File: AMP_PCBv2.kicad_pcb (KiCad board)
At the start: 2 copper layers, 2 parts, among them U1 Teensy4.0, U2 Logo

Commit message: Route PCB
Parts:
- added C1: 47pF, Capacitor_SMD:C_0805_2012Metric_Pad1.18x1.45mm_HandSolder, F.Cu at (145.3, 134.6)
- added C10: 0.1uF, Capacitor_SMD:C_0805_2012Metric_Pad1.18x1.45mm_HandSolder, F.Cu at (177.5, 136.8)
- added C11: 0.1uF, Capacitor_SMD:C_0805_2012Metric_Pad1.18x1.45mm_HandSolder, F.Cu at (178.5, 108.6)
- added C12: 0.1uF, Capacitor_SMD:C_0805_2012Metric_Pad1.18x1.45mm_HandSolder, F.Cu at (181.1, 103.7)
- added C13: 0.1uF, Capacitor_SMD:C_0805_2012Metric_Pad1.18x1.45mm_HandSolder, F.Cu at (109.5, 135.6)
- added C14: 0.1uF, Capacitor_SMD:C_0805_2012Metric_Pad1.18x1.45mm_HandSolder, F.Cu at (138.5, 110.9)
- added C15: 0.1uF, Capacitor_SMD:C_0805_2012Metric_Pad1.18x1.45mm_HandSolder, F.Cu at (138.5, 96.7)
- added C16: 0.1uF, Capacitor_SMD:C_0805_2012Metric_Pad1.18x1.45mm_HandSolder, F.Cu at (164.6, 83.8)
- added C17: 0.1uF, Capacitor_SMD:C_0805_2012Metric_Pad1.18x1.45mm_HandSolder, F.Cu at (156.7, 62.5)
- added C18: 0.1uF, Capacitor_SMD:C_0805_2012Metric_Pad1.18x1.45mm_HandSolder, F.Cu at (176.8, 63.2)
- added C2: 47pF, Capacitor_SMD:C_0805_2012Metric_Pad1.18x1.45mm_HandSolder, F.Cu at (145.3, 136.9)
- added C3: 4.7uF, Capacitor_SMD:C_0805_2012Metric_Pad1.18x1.45mm_HandSolder, F.Cu at (144.9, 131.3)
- added C4: 100nF, Capacitor_SMD:C_0805_2012Metric_Pad1.18x1.45mm_HandSolder, F.Cu at (142.7, 131.3)
- added C5: 100nF, Capacitor_SMD:C_0805_2012Metric_Pad1.18x1.45mm_HandSolder, F.Cu at (140.5, 131.3)
- added C6: 10uF, Capacitor_SMD:C_0805_2012Metric_Pad1.18x1.45mm_HandSolder, F.Cu at (154.7, 94.7)
- added C7: 10uF, Capacitor_SMD:C_0805_2012Metric_Pad1.18x1.45mm_HandSolder, F.Cu at (168.9, 94.7)
- added C8: 10nF, Capacitor_SMD:C_0805_2012Metric_Pad1.18x1.45mm_HandSolder, F.Cu at (156.7, 81.3)
- added C9: 0.1uF, Capacitor_SMD:C_0805_2012Metric_Pad1.18x1.45mm_HandSolder, F.Cu at (180.3, 132.0)
- added D1: GN, LED_THT:LED_D5.0mm, F.Cu at (172.7, 120.1)
- added D10: YL, LED_THT:LED_D5.0mm, F.Cu at (134.6, 88.9)
- added D11: RD, LED_THT:LED_D5.0mm, F.Cu at (134.6, 80.3)
- added D12: RD, LED_THT:LED_D5.0mm, F.Cu at (134.6, 71.6)
- added D13: RD, LED_THT:LED_D5.0mm, F.Cu at (161.0, 68.6)
- added D2: GN, LED_THT:LED_D5.0mm, F.Cu at (179.3, 120.1)
- added D3: GN, LED_THT:LED_D5.0mm, F.Cu at (185.9, 122.6)
- added D4: YL, LED_THT:LED_D5.0mm, F.Cu at (187.7, 94.2)
- added D5: YL, LED_THT:LED_D5.0mm, F.Cu at (187.7, 83.8)
- added D6: YL, LED_THT:LED_D5.0mm, F.Cu at (187.7, 73.4)
- added D7: YL, LED_THT:LED_D5.0mm, F.Cu at (187.7, 63.0)
- added D8: YL, LED_THT:LED_D5.0mm, F.Cu at (148.1, 92.5)
- added D9: YL, LED_THT:LED_D5.0mm, F.Cu at (175.5, 92.5)
- added J1: POWER, Connector_Molex:Molex_Mini-Fit_Jr_5566-02A_2x01_P4.20mm_Vertical, F.Cu at (106.7, 45.7)
- added J2: EBRAKE, Connector_Molex:Molex_Mini-Fit_Jr_5566-02A_2x01_P4.20mm_Vertical, F.Cu at (116.8, 45.7)
- added J3: MC, Connector_Molex:Molex_Mini-Fit_Jr_5566-08A_2x04_P4.20mm_Vertical, F.Cu at (139.6, 51.2)
- added J4: STEERING, Connector_Molex:Molex_Mini-Fit_Jr_5566-08A_2x04_P4.20mm_Vertical, F.Cu at (177.8, 51.2)
- added J5: OLED Breakout, Connector_PinSocket_2.54mm:PinSocket_1x04_P2.54mm_Vertical, F.Cu at (102.4, 124.5)
- added J6: EBRAKE_BREAKOUT, AMP:AMP_Brake_Controller_Breakout, F.Cu at (130.0, 96.2)
- added JP1: 5VOB, Jumper:SolderJumper-2_P1.3mm_Open_TrianglePad1.0x1.5mm, F.Cu at (177.5, 131.7)
- added JP10: Jumper_EBRAKE2, Connector_PinHeader_2.54mm:PinHeader_1x03_P2.54mm_Vertical, F.Cu at (161.6, 101.0)
- added JP11: 0.25s, Jumper:SolderJumper-2_P1.3mm_Open_TrianglePad1.0x1.5mm, F.Cu at (156.5, 65.5)
- added JP12: 1s, Jumper:SolderJumper-2_P1.3mm_Open_TrianglePad1.0x1.5mm, F.Cu at (156.5, 68.3)
- added JP13: 2s, Jumper:SolderJumper-2_P1.3mm_Open_TrianglePad1.0x1.5mm, F.Cu at (156.5, 71.1)
- added JP14: 4s, Jumper:SolderJumper-2_P1.3mm_Open_TrianglePad1.0x1.5mm, F.Cu at (156.5, 73.9)
- added JP2: 3V3OB, Jumper:SolderJumper-2_P1.3mm_Open_TrianglePad1.0x1.5mm, F.Cu at (181.1, 108.8)
- added JP3: Jumper_FS1, Connector_PinHeader_2.54mm:PinHeader_1x03_P2.54mm_Vertical, F.Cu at (161.6, 118.8)
- added JP4: Jumper_FWD, Connector_PinHeader_2.54mm:PinHeader_1x03_P2.54mm_Vertical, F.Cu at (161.6, 116.2)
- added JP5: Jumper_REV, Connector_PinHeader_2.54mm:PinHeader_1x03_P2.54mm_Vertical, F.Cu at (161.6, 113.7)
- added JP6: Jumper_THROTTLE, Connector_PinHeader_2.54mm:PinHeader_1x03_P2.54mm_Vertical, F.Cu at (161.6, 111.2)
- added JP7: Jumper_RB, Connector_PinHeader_2.54mm:PinHeader_1x03_P2.54mm_Vertical, F.Cu at (161.6, 108.6)
- added JP8: Jumper_STEERING, Connector_PinHeader_2.54mm:PinHeader_1x03_P2.54mm_Vertical, F.Cu at (161.6, 106.1)
- added JP9: Jumper_EBRAKE1, Connector_PinHeader_2.54mm:PinHeader_1x03_P2.54mm_Vertical, F.Cu at (161.6, 103.5)
- added JT1: Conn_01x14_Male, Connector_PinHeader_2.54mm:PinHeader_1x14_P2.54mm_Vertical, F.Cu at (132.1, 137.2)
- added JT2: Conn_01x05_Male, Connector_PinHeader_2.54mm:PinHeader_1x05_P2.54mm_Vertical, F.Cu at (124.5, 99.1)
- added JT3: Conn_01x14_Male, Connector_PinHeader_2.54mm:PinHeader_1x14_P2.54mm_Vertical, F.Cu at (106.7, 104.1)
- added JT4: Conn_01x01_Male, Connector_PinHeader_2.54mm:PinHeader_1x01_P2.54mm_Vertical, F.Cu at (104.1, 134.6)
- added JX1: MC_OLD, Connector_Molex:Molex_KK-254_AE-6410-04A_1x04_P2.54mm_Vertical, F.Cu at (147.3, 44.5)
- added Q1: Q_NMOS_GDS, Package_TO_SOT_THT:TO-251-3_Vertical, F.Cu at (181.5, 98.5)
- added Q2: Q_NMOS_GDS, Package_TO_SOT_THT:TO-251-3_Vertical, F.Cu at (181.5, 88.1)
- added Q3: Q_NMOS_GDS, Package_TO_SOT_THT:TO-251-3_Vertical, F.Cu at (181.5, 77.7)
- added Q4: Q_NMOS_GDS, Package_TO_SOT_THT:TO-251-3_Vertical, F.Cu at (181.5, 67.3)
- added R1: 560, Resistor_SMD:R_0805_2012Metric_Pad1.20x1.40mm_HandSolder, F.Cu at (171.4, 117.0)
- added R10: 130, Resistor_SMD:R_0805_2012Metric_Pad1.20x1.40mm_HandSolder, F.Cu at (178.0, 117.0)
- added R11: 56, Resistor_SMD:R_0805_2012Metric_Pad1.20x1.40mm_HandSolder, F.Cu at (184.6, 117.0)
- added R12: 56, Resistor_SMD:R_0805_2012Metric_Pad1.20x1.40mm_HandSolder, F.Cu at (188.7, 98.8)
- added R13: 1K, Resistor_SMD:R_0805_2012Metric_Pad1.20x1.40mm_HandSolder, F.Cu at (184.9, 98.8)
- added R14: 56, Resistor_SMD:R_0805_2012Metric_Pad1.20x1.40mm_HandSolder, F.Cu at (151.6, 87.1)
- added R15: 1K, Resistor_SMD:R_0805_2012Metric_Pad1.20x1.40mm_HandSolder, F.Cu at (154.7, 92.7)
- added R16: 1K, Resistor_SMD:R_0805_2012Metric_Pad1.20x1.40mm_HandSolder, F.Cu at (154.7, 88.1)
- added R17: 56, Resistor_SMD:R_0805_2012Metric_Pad1.20x1.40mm_HandSolder, F.Cu at (188.7, 88.4)
- added R18: 1K, Resistor_SMD:R_0805_2012Metric_Pad1.20x1.40mm_HandSolder, F.Cu at (184.9, 88.4)
- added R19: 1.8K, Resistor_SMD:R_0805_2012Metric_Pad1.20x1.40mm_HandSolder, F.Cu at (154.7, 86.1)
- added R2: 27, Resistor_SMD:R_0805_2012Metric_Pad1.20x1.40mm_HandSolder, F.Cu at (141.2, 134.6)
- added R20: 10K, Resistor_SMD:R_0805_2012Metric_Pad1.20x1.40mm_HandSolder, F.Cu at (138.5, 123.1)
- added R21: 10K, Resistor_SMD:R_0805_2012Metric_Pad1.20x1.40mm_HandSolder, F.Cu at (138.5, 108.9)
- added R22: 56, Resistor_SMD:R_0805_2012Metric_Pad1.20x1.40mm_HandSolder, F.Cu at (188.7, 78.0)
- added R23: 1K, Resistor_SMD:R_0805_2012Metric_Pad1.20x1.40mm_HandSolder, F.Cu at (184.9, 78.0)
- added R24: 56, Resistor_SMD:R_0805_2012Metric_Pad1.20x1.40mm_HandSolder, F.Cu at (172.0, 87.1)
- added R25: 1K, Resistor_SMD:R_0805_2012Metric_Pad1.20x1.40mm_HandSolder, F.Cu at (168.9, 92.7)
- added R26: 1K, Resistor_SMD:R_0805_2012Metric_Pad1.20x1.40mm_HandSolder, F.Cu at (168.9, 88.1)
- added R27: 1.8K, Resistor_SMD:R_0805_2012Metric_Pad1.20x1.40mm_HandSolder, F.Cu at (168.9, 86.1)
- added R28: 56, Resistor_SMD:R_0805_2012Metric_Pad1.20x1.40mm_HandSolder, F.Cu at (188.7, 67.5)
- added R29: 1K, Resistor_SMD:R_0805_2012Metric_Pad1.20x1.40mm_HandSolder, F.Cu at (184.9, 67.5)
- added R3: 10K, Resistor_SMD:R_0805_2012Metric_Pad1.20x1.40mm_HandSolder, F.Cu at (171.4, 131.0)
- added R30: 1K, Resistor_SMD:R_0805_2012Metric_Pad1.20x1.40mm_HandSolder, F.Cu at (181.1, 60.2)
- added R31: 15K, Resistor_SMD:R_0805_2012Metric_Pad1.20x1.40mm_HandSolder, F.Cu at (156.7, 79.2)
- added R32: 6.2K, Resistor_SMD:R_0805_2012Metric_Pad1.20x1.40mm_HandSolder, F.Cu at (156.7, 77.2)
- added R33: 10K, Resistor_SMD:R_0805_2012Metric_Pad1.20x1.40mm_HandSolder, F.Cu at (164.6, 63.2)
- added R34: 10K, Resistor_SMD:R_0805_2012Metric_Pad1.20x1.40mm_HandSolder, F.Cu at (164.6, 73.9)
- added R35: 33, Resistor_SMD:R_0805_2012Metric_Pad1.20x1.40mm_HandSolder, F.Cu at (162.6, 73.9)
- added R36: 33, Resistor_SMD:R_0805_2012Metric_Pad1.20x1.40mm_HandSolder, F.Cu at (134.4, 67.3)
- added R37: 33, Resistor_SMD:R_0805_2012Metric_Pad1.20x1.40mm_HandSolder, F.Cu at (134.4, 75.9)
- added R38: 56, Resistor_SMD:R_0805_2012Metric_Pad1.20x1.40mm_HandSolder, F.Cu at (134.3, 84.6)
- added R4: 10K, Resistor_SMD:R_0805_2012Metric_Pad1.20x1.40mm_HandSolder, F.Cu at (187.2, 109.6)
- added R5: 3.3K, Resistor_SMD:R_0805_2012Metric_Pad1.20x1.40mm_HandSolder, F.Cu at (174.7, 132.0)
- added R6: 6.2K, Resistor_SMD:R_0805_2012Metric_Pad1.20x1.40mm_HandSolder, F.Cu at (183.9, 108.6)
- added R7: 27, Resistor_SMD:R_0805_2012Metric_Pad1.20x1.40mm_HandSolder, F.Cu at (141.2, 136.9)
- added R8: 4.7K, Resistor_SMD:R_0805_2012Metric_Pad1.20x1.40mm_HandSolder, F.Cu at (142.7, 127.0)
- added R9: 10K, Resistor_SMD:R_0805_2012Metric_Pad1.20x1.40mm_HandSolder, F.Cu at (138.7, 127.0)
- added REF**: MountingHole_3.2mm_M3, MountingHole:MountingHole_3.2mm_M3, F.Cu at (96.5, 45.7)
- added REF**: MountingHole_3.2mm_M3, MountingHole:MountingHole_3.2mm_M3, F.Cu at (96.5, 134.6)
- added REF**: MountingHole_3.2mm_M3, MountingHole:MountingHole_3.2mm_M3, F.Cu at (185.4, 45.7)
- added REF**: MountingHole_3.2mm_M3, MountingHole:MountingHole_3.2mm_M3, F.Cu at (185.4, 134.6)
- added U3: LM1117-ADJ, Package_TO_SOT_THT:TO-220-3_Vertical, F.Cu at (172.2, 128.2)
- added U4: LM1117-ADJ, Package_TO_SOT_THT:TO-220-3_Vertical, F.Cu at (186.4, 112.4)
- added U5: 74HC157, Package_DIP:DIP-16_W7.62mm, F.Cu at (138.0, 120.8)
- added U6: 74HC157, Package_DIP:DIP-16_W7.62mm, F.Cu at (138.0, 106.6)
- added U7: 74HC4060, Package_DIP:DIP-16_W7.62mm, F.Cu at (145.8, 63.0)
- added U8: 74HC00, Package_DIP:DIP-14_W7.62mm, F.Cu at (166.9, 63.0)
- added U9: TLV272, Package_DIP:DIP-8_W7.62mm, F.Cu at (158.0, 86.6)
- added USB1: USB_B, Connector_USB:USB_B_TE_5787834_Vertical, F.Cu at (157.0, 128.8)
- U2: value Logo -> FT234XD; footprint AMP:Logo -> Package_DFN_QFN:DFN-12-1EP_3x3mm_P0.5mm_EP1.6x2.5mm
- moved U2 47.2 mm to (136.9, 133.1), turned to 180 degrees
- moved U1 35.9 mm to (119.4, 120.7), turned to 90 degrees
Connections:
- U1 pad 1: unconnected-(U1-Pad1) -> GND
- U1 pad 10: unconnected-(U1-Pad10) -> /MCU_EBRAKE1
- U1 pad 11: unconnected-(U1-Pad11) -> /MCU_EBRAKE2
- U1 pad 12: unconnected-(U1-Pad12) -> Net-(U1-Pad12)
- U1 pad 13: unconnected-(U1-Pad13) -> Net-(U1-Pad13)
- U1 pad 14: unconnected-(U1-Pad14) -> Net-(U1-Pad14)
- U1 pad 15: unconnected-(U1-Pad15) -> Net-(U1-Pad15)
- U1 pad 16: unconnected-(U1-Pad16) -> Net-(U1-Pad16)
- U1 pad 17: unconnected-(U1-Pad17) -> GND
- U1 pad 18: unconnected-(U1-Pad18) -> Net-(U1-Pad18)
- U1 pad 19: unconnected-(U1-Pad19) -> Net-(U1-Pad19)
- U1 pad 2: unconnected-(U1-Pad2) -> /RX1
- U1 pad 20: unconnected-(U1-Pad20) -> Net-(U1-Pad20)
- U1 pad 21: unconnected-(U1-Pad21) -> /WD_SET
- U1 pad 22: unconnected-(U1-Pad22) -> /WD_RESET
- U1 pad 23: unconnected-(U1-Pad23) -> Net-(U1-Pad23)
- U1 pad 24: unconnected-(U1-Pad24) -> Net-(U1-Pad24)
- U1 pad 25: unconnected-(U1-Pad25) -> /OLED_SDA
- U1 pad 26: unconnected-(U1-Pad26) -> /OLED_SCL
- U1 pad 27: unconnected-(U1-Pad27) -> /EBRAKE_EN
- U1 pad 28: unconnected-(U1-Pad28) -> /EBRAKE_IS1
- U1 pad 29: unconnected-(U1-Pad29) -> /EBRAKE_IS2
- U1 pad 3: unconnected-(U1-Pad3) -> /TX1
- U1 pad 30: unconnected-(U1-Pad30) -> Net-(U1-Pad30)
- U1 pad 31: unconnected-(U1-Pad31) -> Net-(U1-Pad31)
- U1 pad 32: unconnected-(U1-Pad32) -> GND
- U1 pad 33: unconnected-(U1-Pad33) -> +5V
- U1 pad 34: unconnected-(U1-Pad34) -> Net-(U1-Pad34)
- U1 pad 4: unconnected-(U1-Pad4) -> /MCU_FS1
- U1 pad 5: unconnected-(U1-Pad5) -> /MCU_FWD
- U1 pad 6: unconnected-(U1-Pad6) -> /MCU_REV
- U1 pad 7: unconnected-(U1-Pad7) -> /MCU_THROTTLE
- U1 pad 8: unconnected-(U1-Pad8) -> /MCU_FB
- U1 pad 9: unconnected-(U1-Pad9) -> /MCU_STEERING
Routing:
- net +5V: track 0.00 -> 201.0 mm, vias 0 -> 1
- net /MUX_FWD: track 0.00 -> 132.9 mm, vias 0 -> 1
- net /MUX_FS1: track 0.00 -> 127.8 mm, vias 0 -> 1
- net /MUX_REV: track 0.00 -> 125.4 mm, vias 0 -> 1
- net +3V3: track 0.00 -> 115.2 mm, vias 0 -> 3
- net /MUX_THROTTLE: track 0.00 -> 108.2 mm, vias 0 -> 3
- net GND: track 0.00 -> 95.4 mm, vias 0 -> 29
- net /MUX_FB: track 0.00 -> 93.4 mm
- net /WD_SET: track 0.00 -> 90.8 mm, vias 0 -> 3
- net /WD_SEL: track 0.00 -> 88.3 mm, vias 0 -> 4
- net /WD_RESET: track 0.00 -> 79.2 mm, vias 0 -> 1
- net /MUX_STEERING: track 0.00 -> 71.5 mm, vias 0 -> 1
- net /MUX_EBRAKE2: track 0.00 -> 66.0 mm
- net /MUX_EBRAKE1: track 0.00 -> 58.6 mm, vias 0 -> 1
- net /EBRAKE_EN: track 0.00 -> 58.4 mm
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- added copper zone on In1.Cu, net +12V
- added copper zone on F.Cu, net /OUT_EBRAKE1
- added copper zone on F.Cu, net /OUT_EBRAKE2
- added copper zone on In2.Cu, net GND
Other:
- board outline added: 99.1 x 99.1 mm
- copper layers 2 -> 4
- board text added: ".25s"
- board text added: "1 2 4"
- board text added: "12V"
- board text added: "1s"
- board text added: "2s"
- board text added: "3V3"
- board text added: "4s"
- board text added: "5V"
- board text added: "EBRAKE1"
- board text added: "EBRAKE2"
- board text added: "EBRAKE_EN"
- board text added: "FB"
- board text added: "FS1"
- board text added: "FWD"
- board text added: "GND"
- board text added: "MUX_FB"
- board text added: "MUX_FS1"
- board text added: "MUX_FWD"
- board text added: "MUX_REV"
- board text added: "MUX_STEERING"
- board text added: "MUX_THROTTLE"
- board text added: "REV"
- board text added: "STEERING"
- board text added: "THROTTLE"
- board text added: "WD"

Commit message: Add logo and label text
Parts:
- added G***: LOGO, AMP:Logo, B.Cu at (112.0, 72.9)
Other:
- board text added: "AMP PCBv2 Revision A 2022-12-23"

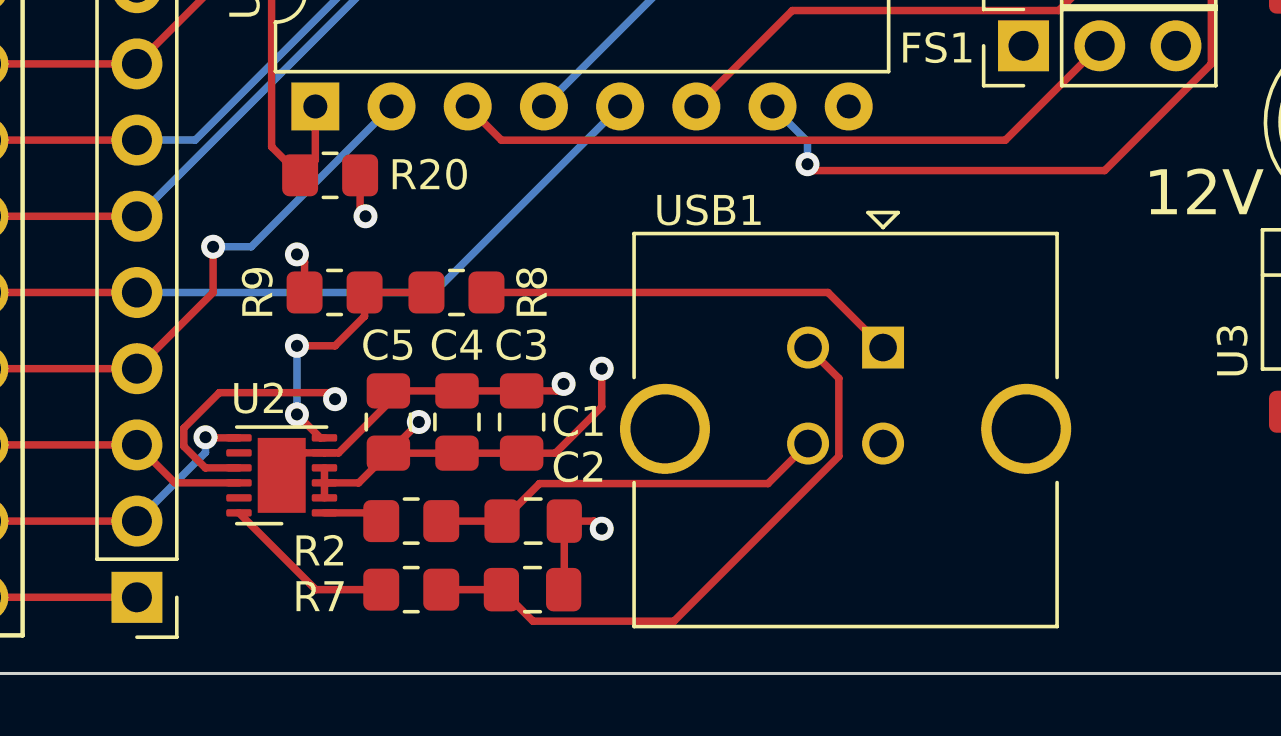
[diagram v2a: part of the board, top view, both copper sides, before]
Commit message: Route differential pair for USB connection
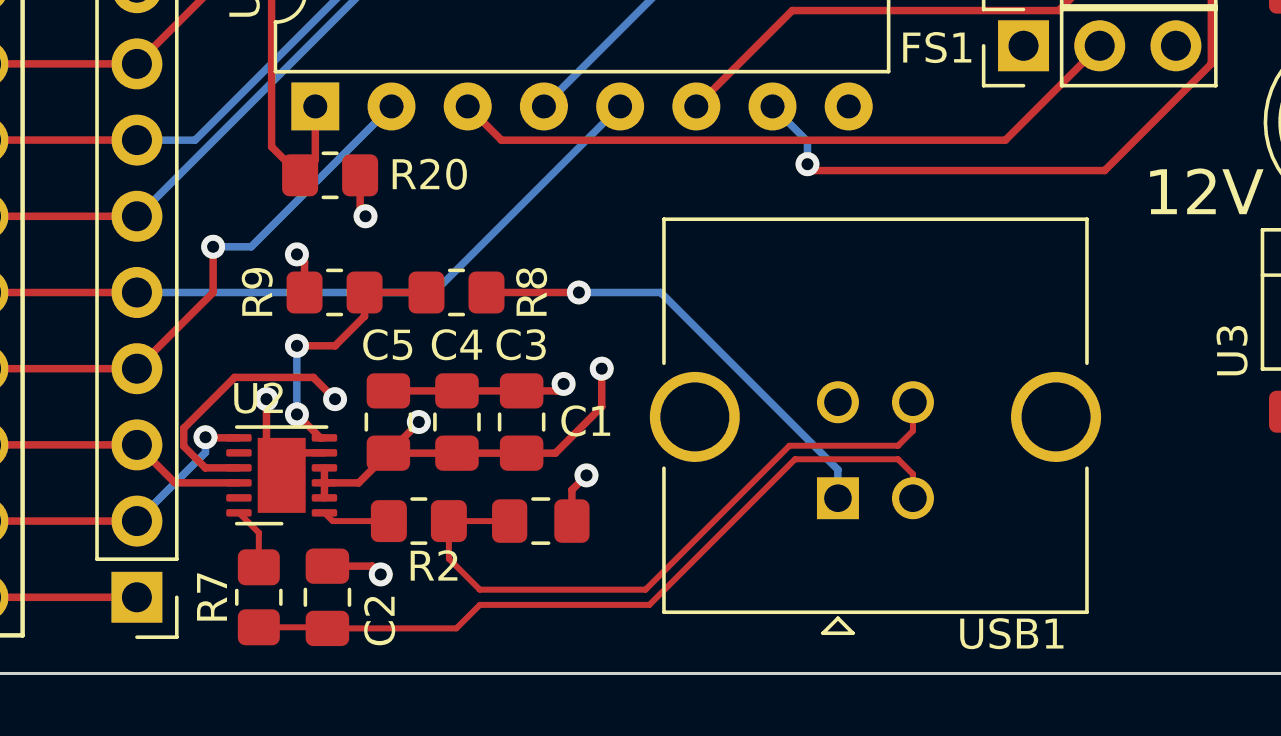
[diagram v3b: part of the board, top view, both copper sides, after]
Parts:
- moved C2 6.84 mm to (138.4, 137.2), turned to 90 degrees
- moved USB1 5.24 mm to (155.4, 133.9), turned to 180 degrees
- moved R7 5.09 mm to (136.1, 137.2), turned to 90 degrees
- moved R2 0.25 mm to (141.5, 134.6)
- moved C1 0.25 mm to (145.5, 134.6)
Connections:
- net Net-(U2-Pad1) renamed /USB_D+
- net Net-(U2-Pad12) renamed /USB_D-
- net Net-(USB1-Pad2) renamed /USB_DR-
- net Net-(USB1-Pad3) renamed /USB_DR+
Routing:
- net /USB_DR+: track 13.3 -> 22.3 mm
- net /USB_DR-: track 20.0 -> 25.2 mm
- net /USB_D-: track 5.80 -> 2.09 mm
- net Net-(R8-Pad1): track 14.0 -> 15.1 mm, vias 0 -> 1
- net GND: track 95.4 -> 94.9 mm, vias 29 -> 31
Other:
- board text added: "AMP PCBv2 Revision A 2022-12-24"
- board text removed: "AMP PCBv2 Revision A 2022-12-23"

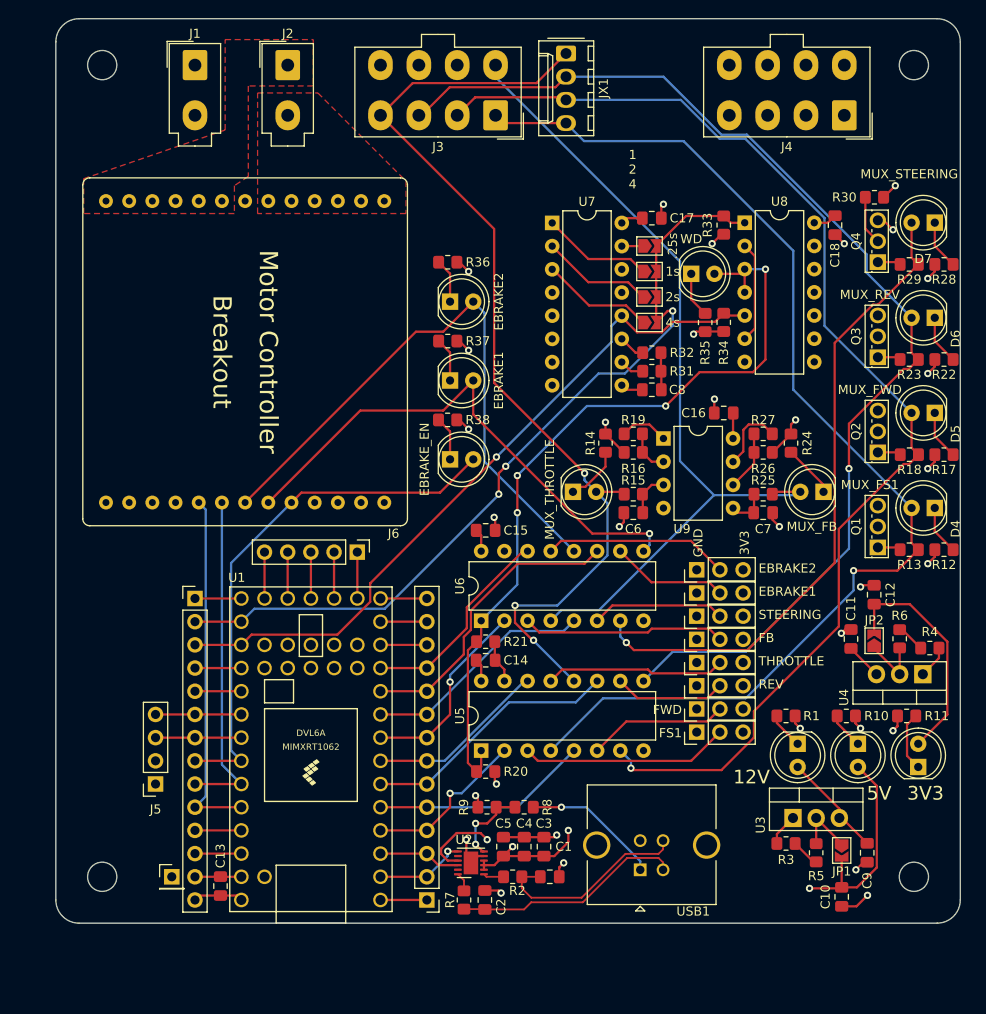
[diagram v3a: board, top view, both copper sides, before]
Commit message: Route new PCB (with LoRa)
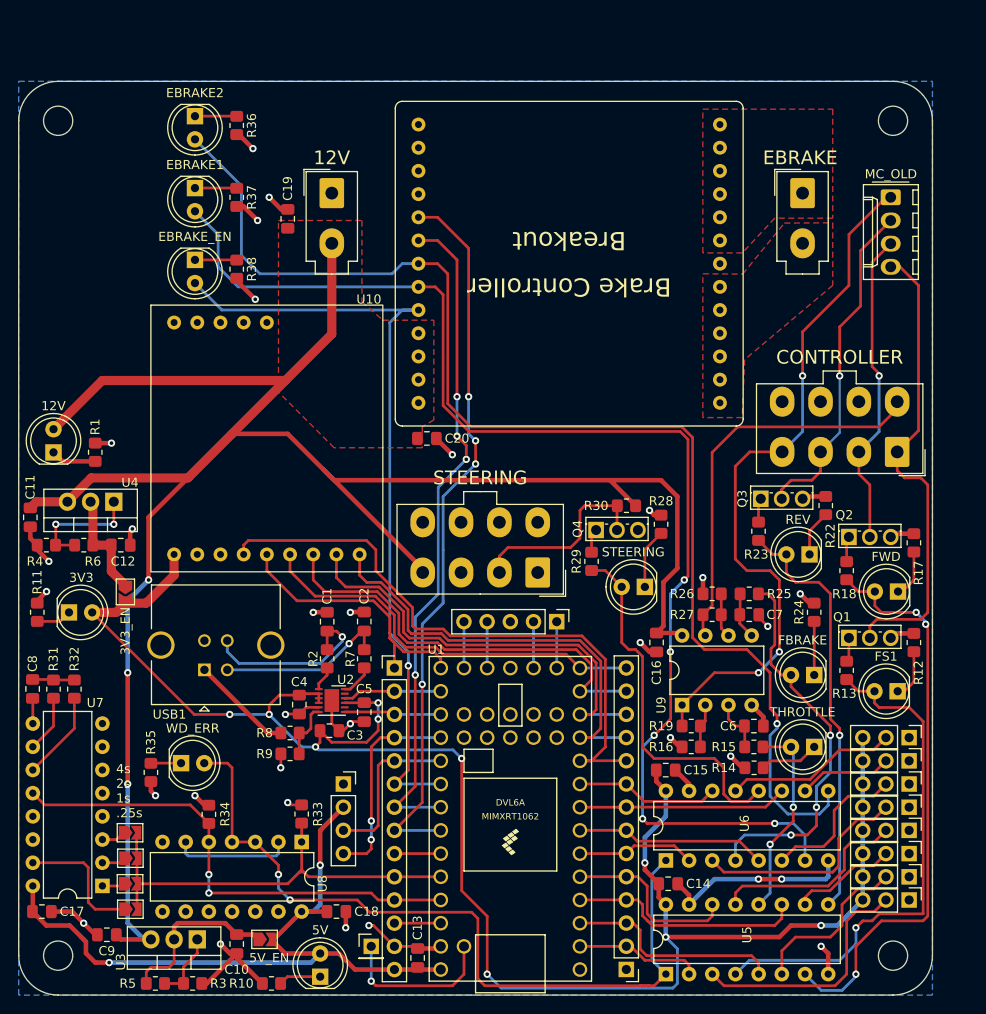
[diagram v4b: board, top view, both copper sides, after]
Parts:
- removed R20, R21: 10K, Resistor_SMD:R_0805_2012Metric_Pad1.20x1.40mm_HandSolder
- removed REF** (x4): MountingHole_3.2mm_M3, MountingHole:MountingHole_3.2mm_M3
- added C19: 10uF, Capacitor_SMD:C_0805_2012Metric_Pad1.18x1.45mm_HandSolder, F.Cu at (116.8, 62.6)
- added C20: 10uF, Capacitor_SMD:C_0805_2012Metric_Pad1.18x1.45mm_HandSolder, F.Cu at (132.1, 86.6)
- added H1: MountingHole, MountingHole:MountingHole_3.2mm_M3, F.Cu at (91.7, 143.3)
- added H2: MountingHole, MountingHole:MountingHole_3.2mm_M3, F.Cu at (183.1, 143.3)
- added H3: MountingHole, MountingHole:MountingHole_3.2mm_M3, F.Cu at (183.1, 51.8)
- added H4: MountingHole, MountingHole:MountingHole_3.2mm_M3, F.Cu at (91.7, 51.8)
- added U10: RFM9x, RF_Module_OTHER:RFM9x_Adafruit, F.Cu at (104.4, 73.9)
- C10, C12: value 0.1uF -> 10uF
- moved C17 101.1 mm to (89.9, 138.4)
- moved R4 97.4 mm to (90.4, 98.3), turned to 0 degrees
- moved R11 95.9 mm to (89.4, 105.6), turned to 90 degrees
- moved D3 94.5 mm to (92.9, 105.7), turned to 0 degrees
- moved C18 92.9 mm to (122.2, 138.4), turned to 0 degrees
- moved JP11 92.3 mm to (99.6, 138.2)
- moved C11 90.9 mm to (88.6, 95.2), turned to -90 degrees
- moved U4 90.6 mm to (97.8, 93.5)
- moved R6 89.9 mm to (94.5, 98.3), turned to 180 degrees
- moved JP12 87.9 mm to (99.6, 135.4)
- moved U7 87.7 mm to (96.5, 135.6), turned to 180 degrees
- moved D1 87.5 mm to (91.2, 88.1), turned to 90 degrees
- moved C9 83.8 mm to (97.0, 141.0), turned to 180 degrees
- moved JP13 83.7 mm to (99.6, 132.6)
- moved U8 83.4 mm to (118.4, 130.8), turned to -90 degrees
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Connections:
- net Net-(JT1-Pad12) renamed /LORA_CS
- net Net-(JT1-Pad13) renamed /LORA_MOSI
- net Net-(JT1-Pad14) renamed /LORA_MISO
- net Net-(JT3-Pad1) renamed /LORA_SCK
- C10 pad 1: +5V -> Net-(C10-Pad1)
- C12 pad 1: +3V3 -> Net-(C12-Pad1)
- C14 pad 1: +12V -> +3V3
- C15 pad 1: +12V -> +3V3
- J3 pad 1: /MUX_FS1 -> /OUT_FS1
- J3 pad 2: /MUX_FWD -> /OUT_FWD
- J3 pad 3: /MUX_REV -> /OUT_REV
- J3 pad 4: /MUX_THROTTLE -> /OUT_THROTTLE
- J3 pad 5: /MUX_FB -> /OUT_FB
- JP1 pad 1: Net-(JP1-Pad1) -> Net-(C10-Pad1)
- JP10 pad 2: /ERR_EBRAKE2 -> /ERR_STEERING
- JP2 pad 1: Net-(JP2-Pad1) -> Net-(C12-Pad1)
- JP8 pad 2: /ERR_STEERING -> /ERR_EBRAKE1
- JP9 pad 2: /ERR_EBRAKE1 -> /ERR_EBRAKE2
- JT1 pad 10: /MCU_EBRAKE1 -> /LORA_INT
- JT1 pad 11: /MCU_EBRAKE2 -> /LORA_RST
- JT1 pad 2: /RX1 -> /MCU_FS1
- JT1 pad 3: /TX1 -> /MCU_FWD
- JT1 pad 4: /MCU_FS1 -> /MCU_REV
- JT1 pad 5: /MCU_FWD -> /MCU_THROTTLE
- JT1 pad 6: /MCU_REV -> /MCU_FB
- JT1 pad 7: /MCU_THROTTLE -> /MCU_EBRAKE1
- JT1 pad 8: /MCU_FB -> /MCU_EBRAKE2
- JT3 pad 10: /EBRAKE_IS2 -> /WD_SET
- JT3 pad 11: Net-(JT3-Pad11) -> /WD_RESET
- JT3 pad 2: /WD_SET -> /USB_UART_TX
- JT3 pad 3: /WD_RESET -> /USB_UART_RX
- JT3 pad 4: Net-(JT3-Pad4) -> /OLED_SDA
- JT3 pad 5: Net-(JT3-Pad5) -> /OLED_SCL
- JT3 pad 6: /OLED_SDA -> /EBRAKE_EN
- JT3 pad 7: /OLED_SCL -> /EBRAKE_IS1
- JT3 pad 8: /EBRAKE_EN -> /EBRAKE_IS2
- JT3 pad 9: /EBRAKE_IS1 -> Net-(JT3-Pad9)
- JX1 pad 1: /MUX_THROTTLE -> /OUT_THROTTLE
- JX1 pad 2: /MUX_REV -> /OUT_REV
- JX1 pad 3: /MUX_FWD -> /OUT_FWD
- JX1 pad 4: /MUX_FS1 -> /OUT_FS1
- Q4 pad 2: /OUT_Steering -> /STEERING_INPUT_B+
- R30 pad 1: /OUT_Steering -> /STEERING_INPUT_B+
- R5 pad 1: Net-(JP1-Pad1) -> Net-(C10-Pad1)
- R6 pad 1: Net-(JP2-Pad1) -> Net-(C12-Pad1)
- U1 pad 10: /MCU_EBRAKE1 -> /LORA_INT
- U1 pad 11: /MCU_EBRAKE2 -> /LORA_RST
- U1 pad 2: /RX1 -> /MCU_FS1
- U1 pad 21: /WD_SET -> /USB_UART_TX
- U1 pad 22: /WD_RESET -> /USB_UART_RX
- U1 pad 23: Net-(JT3-Pad4) -> /OLED_SDA
- U1 pad 24: Net-(JT3-Pad5) -> /OLED_SCL
- U1 pad 25: /OLED_SDA -> /EBRAKE_EN
- U1 pad 26: /OLED_SCL -> /EBRAKE_IS1
- U1 pad 27: /EBRAKE_EN -> /EBRAKE_IS2
- U1 pad 28: /EBRAKE_IS1 -> Net-(JT3-Pad9)
- U1 pad 29: /EBRAKE_IS2 -> /WD_SET
- U1 pad 3: /TX1 -> /MCU_FWD
- U1 pad 30: Net-(JT3-Pad11) -> /WD_RESET
- U1 pad 4: /MCU_FS1 -> /MCU_REV
- U1 pad 5: /MCU_FWD -> /MCU_THROTTLE
- U1 pad 6: /MCU_REV -> /MCU_FB
- U1 pad 7: /MCU_THROTTLE -> /MCU_EBRAKE1
- U1 pad 8: /MCU_FB -> /MCU_EBRAKE2
- U2 pad 10: /TX1 -> /USB_UART_TX
- U2 pad 7: /RX1 -> /USB_UART_RX
- U3 pad 1: GND -> Net-(R3-Pad2)
- U3 pad 2: Net-(JP1-Pad1) -> Net-(C10-Pad1)
- U4 pad 1: GND -> Net-(R4-Pad2)
- U4 pad 2: Net-(JP2-Pad1) -> Net-(C12-Pad1)
- U5 pad 16: +12V -> +3V3
- U6 pad 10: /ERR_EBRAKE1 -> /ERR_EBRAKE2
- U6 pad 11: /MCU_EBRAKE1 -> /MCU_EBRAKE2
- U6 pad 12: /MUX_EBRAKE2 -> /MUX_STEERING
- U6 pad 13: /ERR_EBRAKE2 -> /ERR_STEERING
- U6 pad 14: /MCU_EBRAKE2 -> /MCU_STEERING
- U6 pad 16: +12V -> +3V3
- U6 pad 5: /MCU_STEERING -> /MCU_EBRAKE1
- U6 pad 6: /ERR_STEERING -> /ERR_EBRAKE1
- U6 pad 7: /MUX_STEERING -> /MUX_EBRAKE1
- U6 pad 9: /MUX_EBRAKE1 -> /MUX_EBRAKE2
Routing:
- net +12V: track 25.3 -> 227.3 mm, vias 1 -> 3
- net +5V: track 201.0 -> 79.4 mm, vias 1 -> 2
- net /MUX_THROTTLE: track 108.2 -> 22.0 mm, vias 3 -> 2
- net +3V3: track 115.6 -> 198.4 mm, vias 3 -> 10
- net /MUX_EBRAKE1: track 58.6 -> 138.5 mm, vias 1 -> 5
- net /MUX_REV: track 125.4 -> 46.5 mm
- net /OUT_THROTTLE: track 5.36 -> 78.1 mm, vias 0 -> 3
- net /MUX_FS1: track 127.8 -> 56.4 mm
- net /MUX_EBRAKE2: track 66.0 -> 137.0 mm, vias 0 -> 1
- net /MUX_FWD: track 132.9 -> 63.3 mm, vias 1 -> 3
- net /LORA_INT: track 0.00 -> 66.9 mm
- net /OUT_FS1: track 0.00 -> 51.4 mm
- net /MUX_FB: track 93.4 -> 42.3 mm, vias 0 -> 3
- net /LORA_RST: track 0.00 -> 49.1 mm
- net /LORA_CS: track 5.08 -> 48.4 mm
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- added copper zone on F.Cu, net +12V
- added copper zone on B.Cu, net GND
- removed copper zone on In1.Cu, net +12V
- removed copper zone on In2.Cu, net GND
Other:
- board size 99.1 x 99.1 mm -> 100.1 x 100.1 mm
- copper layers 4 -> 2
- board text added: "3V3_EN"
- board text added: "4s 2s 1s .25s"
- board text added: "5V_EN"
- board text added: "AMP PCBv2 Revision A 2022-12-26"
- board text added: "CONTROLLER"
- board text added: "EBRAKE"
- board text added: "FBRAKE"
- board text added: "MC_OLD"
- board text added: "WD_ERR"
- board text removed: ".25s"
- board text removed: "1 2 4"
- board text removed: "1s"
- board text removed: "2s"
- board text removed: "4s"
- board text removed: "AMP PCBv2 Revision A 2022-12-24"
- board text removed: "FB"
- board text removed: "GND"
- board text removed: "MUX_FB"
- board text removed: "MUX_FS1"
- board text removed: "MUX_FWD"
- board text removed: "MUX_REV"
- board text removed: "MUX_STEERING"
- board text removed: "MUX_THROTTLE"
- board text removed: "WD"
